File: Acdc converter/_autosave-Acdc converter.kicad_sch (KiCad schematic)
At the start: 15 parts, among them J1 Conn_01x03, J2 Conn_01x03, U1 LM7812_TO220, U2 LM7812_TO220

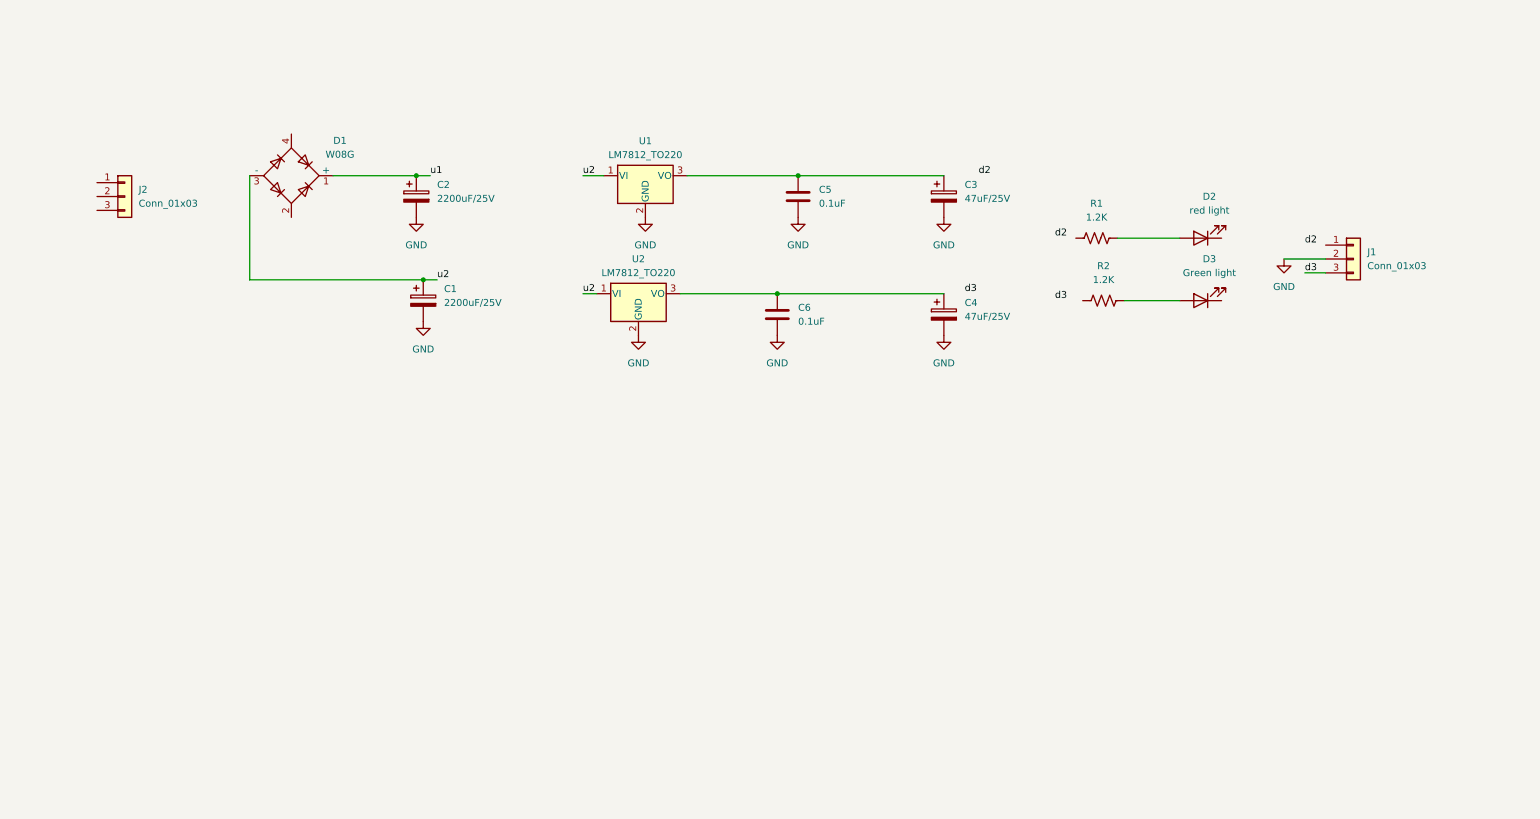
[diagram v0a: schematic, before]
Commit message: :sparkles: added stepdown transformer
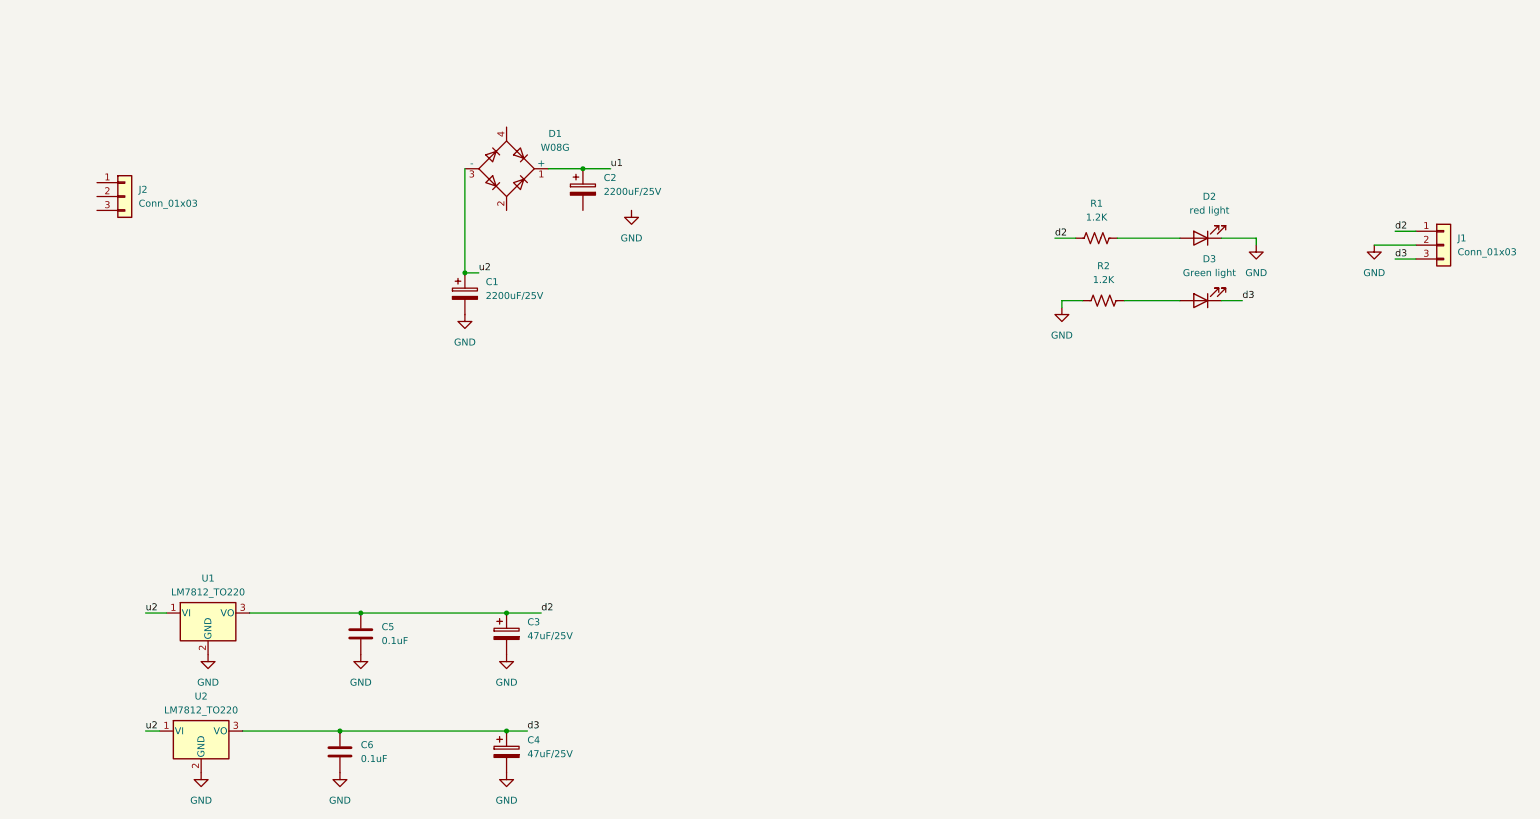
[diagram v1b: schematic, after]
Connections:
- net GND: now also D2.1 (K), R2.1; no longer C2.2
- net d2: now also C3.1, C5.1, J1.1 (Pin_1), R1.1, U1.3 (VO)
- net d3: now also C4.1, C6.1, D3.1 (K), U2.3 (VO)
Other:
- moved on the sheet: C1, C2, C3, C4, C5, C6, D1, J1, U1, U2

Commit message: :memo : labelled circuit diagram
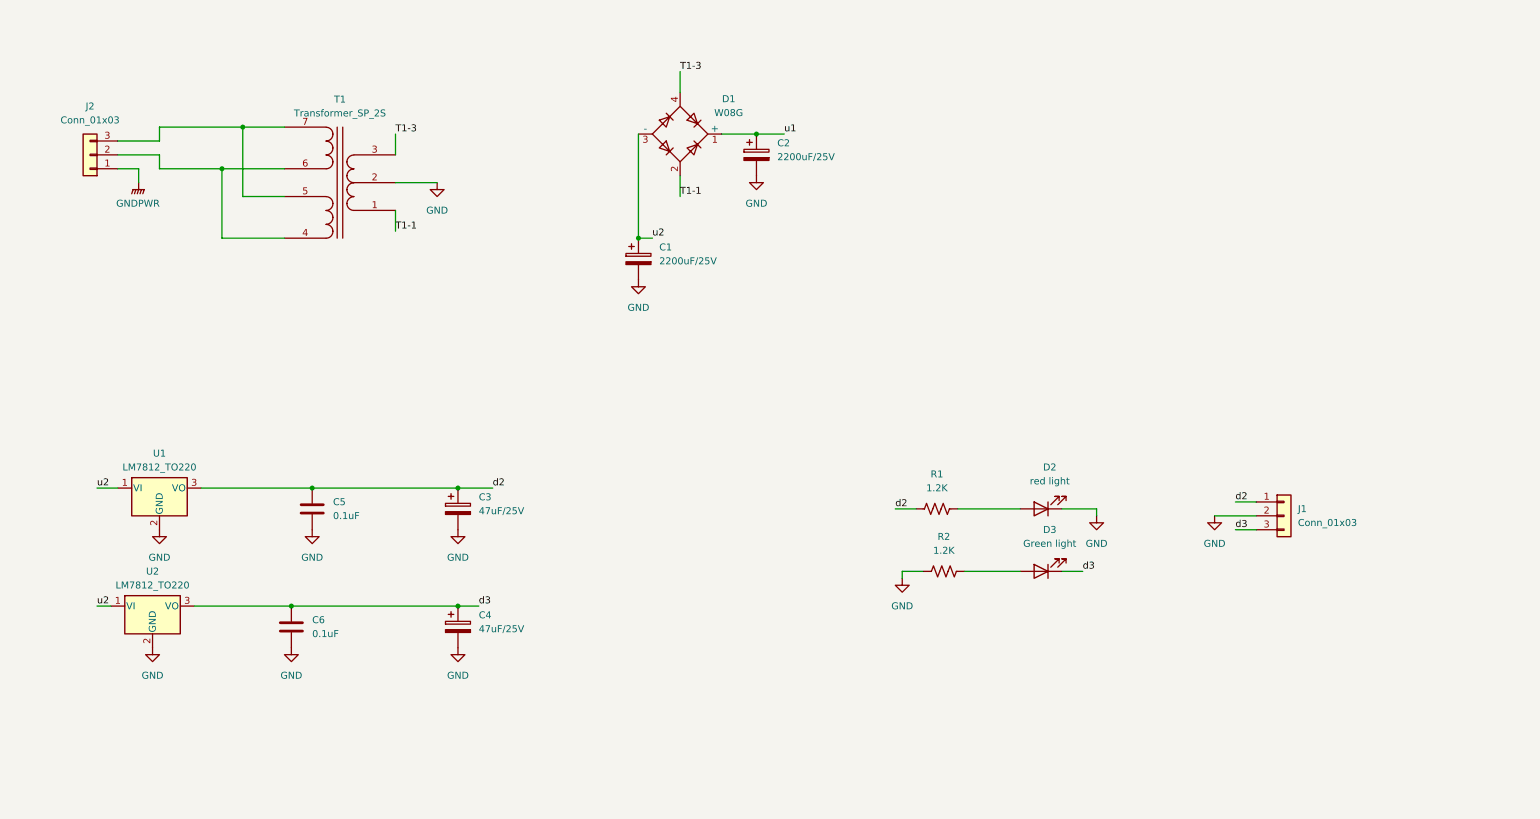
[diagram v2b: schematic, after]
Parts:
- added T1: Transformer_SP_2S, symbol Device:Transformer_SP_2S
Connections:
- net GND: now also C2.2, T1.2 (PM)
- net GNDPWR: now reaches J2.1 (Pin_1)
- net at J2.2 (Pin_2): now also T1.4 (OUT1A), T1.6 (OUT2A)
- net at J2.3 (Pin_3): now also T1.5 (OUT1B), T1.7 (OUT2B)
- net T1-1: now reaches D1.2
- net T1-1: now also T1.1 (IN+)
- net T1-3: now reaches D1.4
- net T1-3: now also T1.3 (IN-)
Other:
- moved on the sheet: C1, C2, C3, C4, C5, C6, D1, D2, D3, J1, J2, R1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

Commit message: :construction: placed components on editor
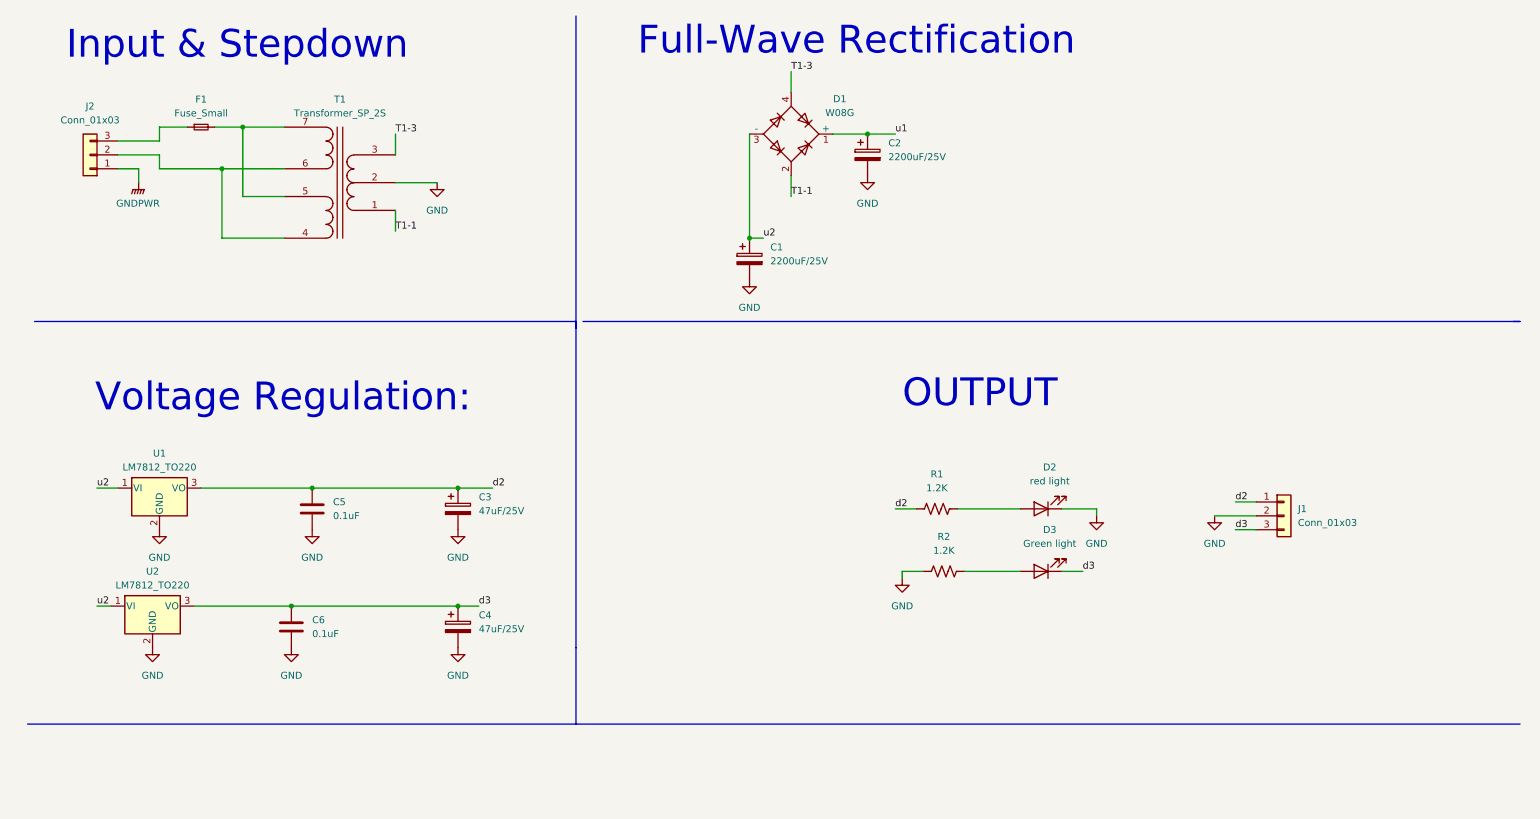
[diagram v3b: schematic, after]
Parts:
- added F1: Fuse_Small, Fuse:Fuseholder_Cylinder-5x20mm_EATON_HBW_Vertical_Closed, symbol Device:Fuse_Small
- J1, J2: footprint (none) -> Connector_Phoenix_GMSTB:PhoenixContact_GMSTBA_2,5_3-G-7,62_1x03_P7.62mm_Horizontal
- R1, R2: footprint (none) -> Resistor_SMD:R_0201_0603Metric_Pad0.64x0.40mm_HandSolder
- T1: footprint (none) -> Transformer_THT:Transformer_CHK_EI30-2VA_1xSec
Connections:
- net at T1.5 (OUT1B), T1.7 (OUT2B): now also F1.2; no longer J2.3 (Pin_3)
- new net: F1.1, J2.3 (Pin_3)
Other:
- note added: "Full-Wave Rectification"
- note added: "Input & Stepdown"
- note added: "OUTPUT"
- note added: "Voltage Regulation:"
- moved on the sheet: C1, C2, D1
